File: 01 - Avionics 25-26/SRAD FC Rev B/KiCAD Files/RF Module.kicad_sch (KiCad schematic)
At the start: 0 parts

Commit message: Import CAD Files to make project symbol
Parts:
- added U2: SX1276IMLTRT, SX1276IMLTRT:QFN65P600X600X100-29N, symbol SX1276IMLTRT:SX1276IMLTRT
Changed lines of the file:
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@@
 	(generator_version "9.0")
 	(paper "A4")
+	(symbol
+		(lib_id "SX1276IMLTRT:SX1276IMLTRT")
+		(at 135.89 101.6 0)
+		(unit 1)
+		(exclude_from_sim no)
+		(in_bom yes)
+		(on_board yes)
+		(dnp no)
+		(fields_autoplaced yes)
+		(property "Reference" "U2"
+			(at 135.89 63.5 0)
+			(effects
+				(font
+					(size 1.27 1.27)
+				)
+			)
+		)
+		(property "Value" "SX1276IMLTRT"
+			(at 135.89 66.04 0)
+			(effects
+				(font
+					(size 1.27 1.27)
+				)
+			)
+		)
+		(property "Footprint" "SX1276IMLTRT:QFN65P600X600X100-29N"
+			(at 135.89 101.6 0)
+			(effects
+				(font
+					(size 1.27 1.27)
+				)
+				(justify bottom)
+				(hide yes)
+			)
+		)
+		(property "Datasheet" ""
+			(at 135.89 101.6 0)
+			(effects
+				(font
+					(size 1.27 1.27)
+				)
+				(hide yes)
+			)
+		)
+		(property "Description" ""
+			(at 135.89 101.6 0)
+			(effects
+				(font
+					(size 1.27 1.27)
+				)
+				(hide yes)
+			)
+		)
+		(property "PARTREV" "5"
+			(at 135.89 101.6 0)
+			(effects
+				(font
+					(size 1.27 1.27)
+				)
+				(justify bottom)
+				(hide yes)
+			)
+		)
+		(property "MANUFACTURER" "Semtech Corporation"
+			(at 135.89 101.6 0)
+			(effects
+				(font
+					(size 1.27 1.27)
+				)
+				(justify bottom)
+				(hide yes)
+			)
+		)
+		(property "STANDARD" "IPC-7351B"
+			(at 135.89 101.6 0)
+			(effects
+				(font
+					(size 1.27 1.27)
+				)
+				(justify bottom)
+				(hide yes)
+			)
+		)
+		(pin "29"
+		)
+		(pin "17"
+		)
+		(pin "18"
+		)
+		(pin "16"
+		)
+		(pin "1"
+		)
+		(pin "21"
+		)
+		(pin "7"
+		)
+		(pin "19"
+		)
+		(pin "27"
+		)
+		(pin "23"
+		)
+		(pin "26"
+		)
+		(pin "9"
+		)
+		(pin "6"
+		)
+		(pin "24"
+		)
+		(pin "12"
+		)
+		(pin "11"
+		)
+		(pin "10"
+		)
+		(pin "5"
+		)
+		(pin "3"
+		)
+		(pin "2"
+		)
+		(pin "15"
+		)
+		(pin "28"
+		)
+		(pin "14"
+		)
+		(pin "8"
+		)
+		(pin "20"
+		)
+		(pin "4"
+		)
+		(pin "25"
+		)
+		(pin "22"
+		)
+		(pin "13"
+		)
+		(instances
+			(project ""
+				(path "/1dd9e63a-24f2-43c6-ae21-66b89e6998f2/c560a1ce-e177-4cce-a057-3c7d08124339"
+					(reference "U2")
+					(unit 1)
+				)
+			)
+		)
+	)
 )

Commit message: Info to Storage and RF Module
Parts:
- RFModule: renamed from U2; Link (none) -> https://www.digikey.com/en/products/detail/semtech-corporat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
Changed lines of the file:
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@@
 		(dnp no)
 		(fields_autoplaced yes)
-		(property "Reference" "U2"
+		(property "Reference" "RFModule"
 			(at 135.89 63.5 0)
 			(effects
@@
 			)
 		)
-		(property "Datasheet" ""
+		(property "Datasheet" "https://semtech.my.salesforce.com/sfc/p/#E0000000JelG/a/2R0000001OKs/Bs97dmPXeatnbdoJNVMIDaKDlQz8q1N_gxDcgqi7g2o"
 			(at 135.89 101.6 0)
 			(effects
@@
 			)
 		)
-		(property "Description" ""
+		(property "Description" "SX1276/77/78/79 - 137 MHz to 1020 MHz Low Power Long Range Transceiver"
+			(at 135.89 101.6 0)
+			(effects
+				(font
+					(size 1.27 1.27)
+				)
+				(hide yes)
+			)
+		)
+		(property "Link" "https://www.digikey.com/en/products/detail/semtech-corporation/SX1276IMLTRT/4259565"
 			(at 135.89 101.6 0)
 			(effects
@@
 			(project ""
 				(path "/1dd9e63a-24f2-43c6-ae21-66b89e6998f2/c560a1ce-e177-4cce-a057-3c7d08124339"
-					(reference "U2")
+					(reference "RFModule")
 					(unit 1)
 				)

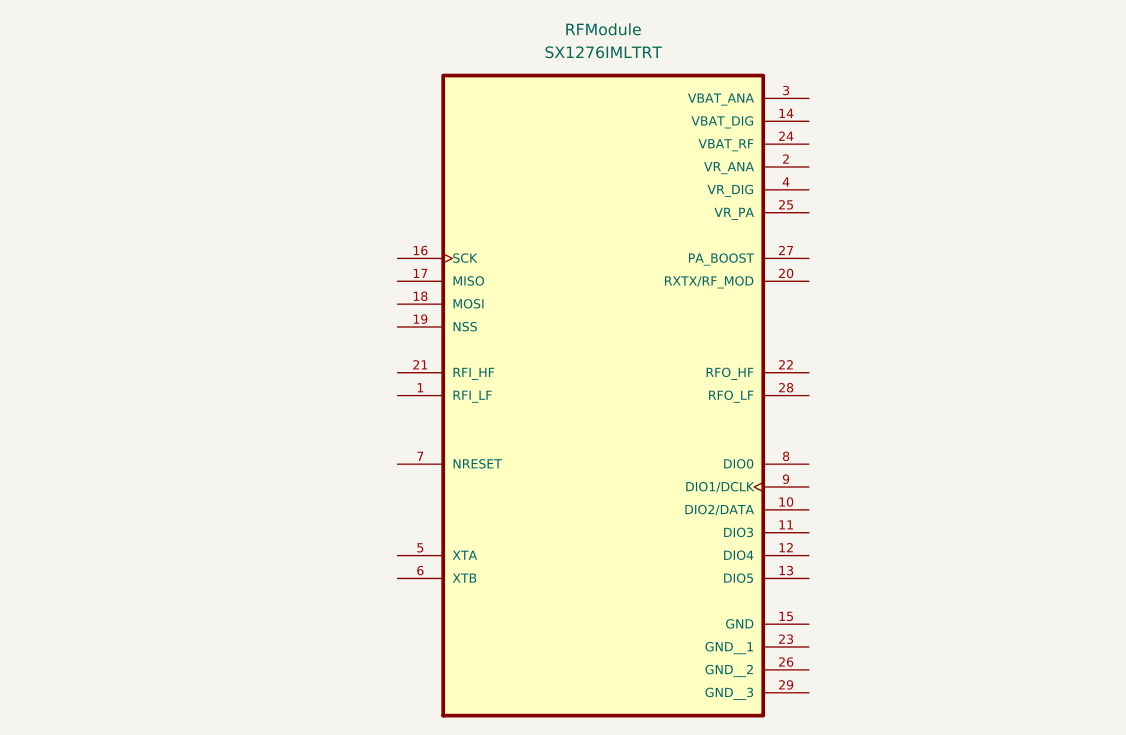
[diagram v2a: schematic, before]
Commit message: Added Storage and RF Module Circuits with Labels for Future Connects
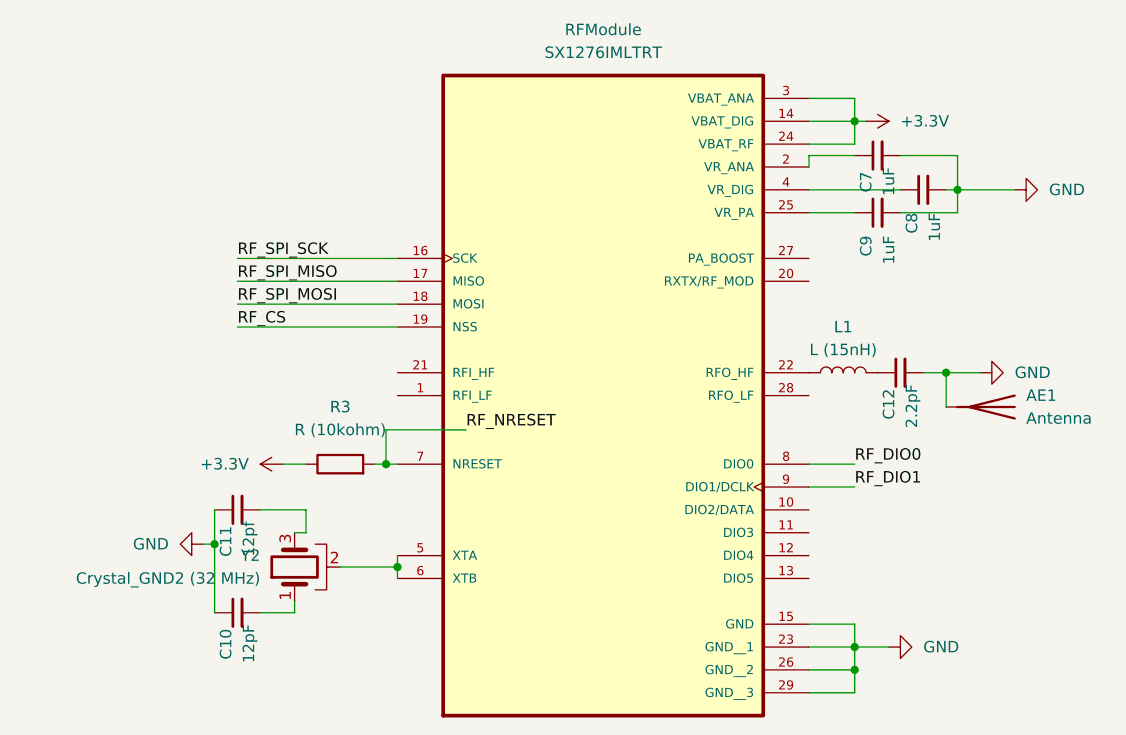
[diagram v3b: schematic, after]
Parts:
- added AE1: Antenna, symbol Device:Antenna
- added C10: 12pF, symbol Device:C_Small
- added C11: 12pf, symbol Device:C_Small
- added C12: 2.2pF, symbol Device:C_Small
- added C7, C8, C9: 1uF, symbol Device:C_Small
- added L1: L (15nH), symbol Device:L
- added R3: R (10kohm), symbol Device:R
- added Y2: Crystal_GND2 (32 MHz), symbol Device:Crystal_GND2
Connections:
- net +3.3V: now reaches RFModule.14 (VBAT_DIG)
- net +3.3V: now also RFModule.24 (VBAT_RF), RFModule.3 (VBAT_ANA), R3.1
- net GND: now reaches RFModule.15 (GND)
- net GND: now also RFModule.23 (GND__1), RFModule.26 (GND__2), RFModule.29 (GND__3), AE1.1 (A), C10.1, C11.1, C12.2, C7.2, C8.2, C9.2
- net RF_SPI_SCK: now reaches RFModule.16 (SCK)
- net RF_SPI_MISO: now reaches RFModule.17 (MISO)
- net RF_SPI_MOSI: now reaches RFModule.18 (MOSI)
- net RF_CS: now reaches RFModule.19 (NSS)
- net at RFModule.2 (VR_ANA): now also C7.1
- net at RFModule.22 (RFO_HF): now also L1.1
- net at RFModule.25 (VR_PA): now also C9.1
- net at RFModule.4 (VR_DIG): now also C8.1
- net at RFModule.5 (XTA): now also RFModule.6 (XTB), Y2.2
- net RF_NRESET: now reaches RFModule.7 (NRESET)
- net RF_NRESET: now also R3.2
- net RF_DIO0: now reaches RFModule.8 (DIO0)
- net RF_DIO1: now reaches RFModule.9 (DIO1/DCLK)
- new net: C11.2, Y2.3
- new net: C12.1, L1.2
- new net: C10.2, Y2.1

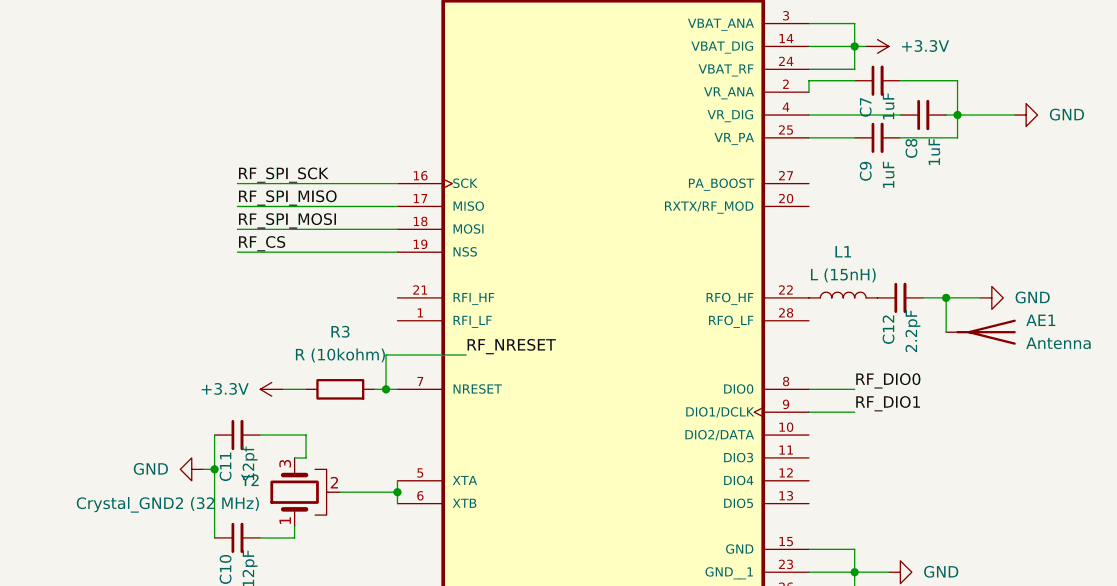
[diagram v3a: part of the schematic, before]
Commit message: Updated Sheet Pins
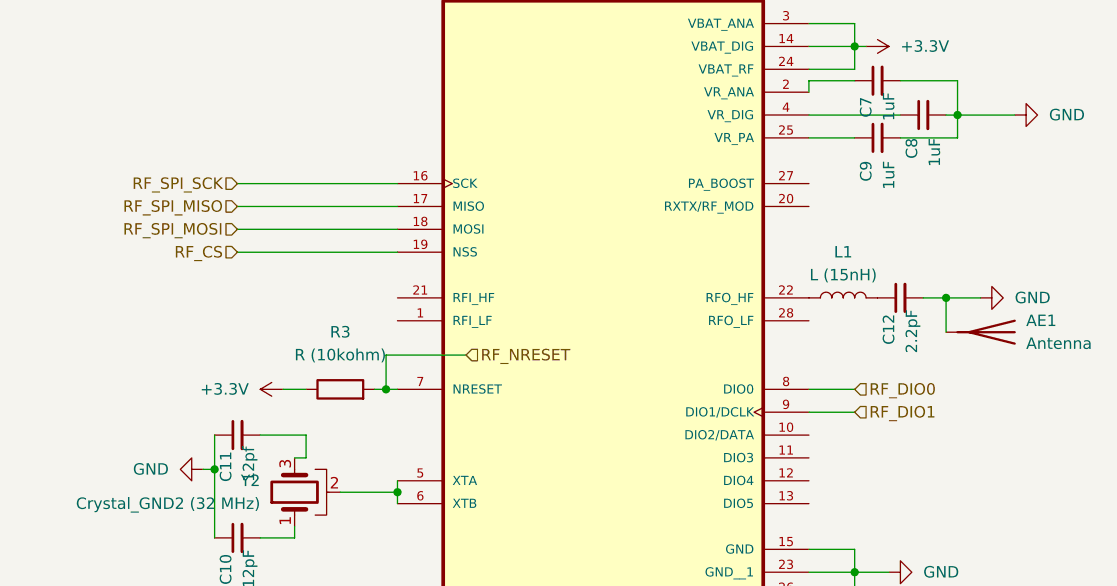
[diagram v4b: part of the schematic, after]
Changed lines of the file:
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@@
 		)
 	)
-	(label "RF_DIO0"
+	(hierarchical_label "RF_CS"
+		(shape input)
+		(at 95.25 96.52 180)
+		(effects
+			(font
+				(size 1.27 1.27)
+			)
+			(justify right)
+		)
+	)
+	(hierarchical_label "RF_DIO1"
+		(shape input)
+		(at 163.83 114.3 0)
+		(effects
+			(font
+				(size 1.27 1.27)
+			)
+			(justify left)
+		)
+	)
+	(hierarchical_label "RF_SPI_MOSI"
+		(shape input)
+		(at 95.25 93.98 180)
+		(effects
+			(font
+				(size 1.27 1.27)
+			)
+			(justify right)
+		)
+	)
+	(hierarchical_label "RF_DIO0"
+		(shape input)
 		(at 163.83 111.76 0)
 		(effects
@@
 				(size 1.27 1.27)
 			)
-			(justify left bottom)
+			(justify left)
 		)
 	)
-	(label "RF_CS"
-		(at 95.25 96.52 0)
+	(hierarchical_label "RF_SPI_SCK"
+		(shape input)
+		(at 95.25 88.9 180)
 		(effects
 			(font
 				(size 1.27 1.27)
 			)
-			(justify left bottom)
+			(justify right)
 		)
 	)
-	(label "RF_SPI_SCK"
-		(at 95.25 88.9 0)
+	(hierarchical_label "RF_SPI_MISO"
+		(shape input)
+		(at 95.25 91.44 180)
 		(effects
 			(font
 				(size 1.27 1.27)
 			)
-			(justify left bottom)
+			(justify right)
 		)
 	)
-	(label "RF_DIO1"
-		(at 163.83 114.3 0)
-		(effects
-			(font
-				(size 1.27 1.27)
-			)
-			(justify left bottom)
-		)
-	)
-	(label "RF_SPI_MISO"
-		(at 95.25 91.44 0)
-		(effects
-			(font
-				(size 1.27 1.27)
-			)
-			(justify left bottom)
-		)
-	)
-	(label "RF_NRESET"
+	(hierarchical_label "RF_NRESET"
+		(shape input)
 		(at 120.65 107.95 0)
 		(effects
@@
 				(size 1.27 1.27)
 			)
-			(justify left bottom)
+			(justify left)
 		)
 	)
-	(label "RF_SPI_MOSI"
-		(at 95.25 93.98 0)
-		(effects
-			(font
-				(size 1.27 1.27)
-			)
-			(justify left bottom)
-		)
-	)

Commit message: added power as hierarchical sheet pins
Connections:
- net +3.3V renamed RF_3.3V_POWER
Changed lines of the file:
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@@
+	)
+	(junction
+		(at 134.62 151.13)
+		(diameter 0)
+		(color 0 0 0 0)
 	)
 	(junction
@@
 	(wire
 		(pts
-			(xy 100.33 111.76) (xy 102.87 111.76)
-		)
-		(stroke
-			(width 0)
-			(type default)
-		)
-	)
-	(wire
-		(pts
 			(xy 111.76 107.95) (xy 111.76 111.76)
 		)
@@
 	(wire
 		(pts
+			(xy 199.39 151.13) (xy 134.62 151.13)
+		)
+		(stroke
+			(width 0)
+			(type default)
+		)
+	)
+	(wire
+		(pts
 			(xy 97.79 116.84) (xy 102.87 116.84)
 		)
@@
 	(wire
 		(pts
-			(xy 165.1 73.66) (xy 163.83 73.66)
+			(xy 163.83 73.66) (xy 199.39 73.66)
 		)
 		(stroke
@@
 	(wire
 		(pts
+			(xy 52.07 111.76) (xy 52.07 151.13)
+		)
+		(stroke
+			(width 0)
+			(type default)
+		)
+	)
+	(wire
+		(pts
 			(xy 91.44 120.65) (xy 92.71 120.65)
 		)
@@
 	(wire
 		(pts
+			(xy 199.39 73.66) (xy 199.39 151.13)
+		)
+		(stroke
+			(width 0)
+			(type default)
+		)
+	)
+	(wire
+		(pts
 			(xy 163.83 71.12) (xy 163.83 73.66)
 		)
@@
 	(wire
 		(pts
+			(xy 52.07 151.13) (xy 134.62 151.13)
+		)
+		(stroke
+			(width 0)
+			(type default)
+		)
+	)
+	(wire
+		(pts
+			(xy 52.07 111.76) (xy 102.87 111.76)
+		)
+		(stroke
+			(width 0)
+			(type default)
+		)
+	)
+	(wire
+		(pts
 			(xy 92.71 116.84) (xy 92.71 120.65)
 		)
@@
 		(pts
 			(xy 106.68 123.19) (xy 113.03 123.19)
+		)
+		(stroke
+			(width 0)
+			(type default)
+		)
+	)
+	(wire
+		(pts
+			(xy 134.62 151.13) (xy 134.62 161.29)
 		)
 		(stroke
@@
 		(shape input)
 		(at 95.25 96.52 180)
+		(effects
+			(font
+				(size 1.27 1.27)
+			)
+			(justify right)
+		)
+	)
+	(hierarchical_label "RF_3.3V_POWER"
+		(shape input)
+		(at 134.62 161.29 270)
 		(effects
 			(font
@@
 	)
 	(symbol
-		(lib_id "power:+3.3V")
-		(at 165.1 73.66 270)
-		(unit 1)
-		(exclude_from_sim no)
-		(in_bom yes)
-		(on_board yes)
-		(dnp no)
-		(fields_autoplaced yes)
-		(property "Reference" "#PWR013"
-			(at 161.29 73.66 0)
-			(effects
-				(font
-					(size 1.27 1.27)
-				)
-				(hide yes)
-			)
-		)
-		(property "Value" "+3.3V"
-			(at 168.91 73.6599 90)
-			(effects
-				(font
-					(size 1.27 1.27)
-				)
-				(justify left)
-			)
-		)
-		(property "Footprint" ""
-			(at 165.1 73.66 0)
-			(effects
-				(font
-					(size 1.27 1.27)
-				)
-				(hide yes)
-			)
-		)
-		(property "Datasheet" ""
-			(at 165.1 73.66 0)
-			(effects
-				(font
-					(size 1.27 1.27)
-				)
-				(hide yes)
-			)
-		)
-		(property "Description" "Power symbol creates a global label with name \"+3.3V\""
-			(at 165.1 73.66 0)
-			(effects
-				(font
-					(size 1.27 1.27)
-				)
-				(hide yes)
-			)
-		)
-		(pin "1"
-		)
-		(instances
-			(project ""
-				(path "/1dd9e63a-24f2-43c6-ae21-66b89e6998f2/c560a1ce-e177-4cce-a057-3c7d08124339"
-					(reference "#PWR013")
-					(unit 1)
-				)
-			)
-		)
-	)
-	(symbol
 		(lib_id "Device:Crystal_GND2")
 		(at 101.6 123.19 90)
@@
 					(unit 1)
 				)
-			)
-		)
-	)
-	(symbol
-		(lib_id "power:+3.3V")
-		(at 100.33 111.76 90)
-		(unit 1)
-		(exclude_from_sim no)
-		(in_bom yes)
-		(on_board yes)
-		(dnp no)
-		(fields_autoplaced yes)
-		(property "Reference" "#PWR017"
-			(at 104.14 111.76 0)
-			(effects
-				(font
-					(size 1.27 1.27)
-				)
-				(hide yes)
-			)
-		)
-		(property "Value" "+3.3V"
-			(at 96.52 111.7599 90)
-			(effects
-				(font
-					(size 1.27 1.27)
-				)
-				(justify left)
-			)
-		)
-		(property "Footprint" ""
-			(at 100.33 111.76 0)
-			(effects
-				(font
-					(size 1.27 1.27)
-				)
-				(hide yes)
-			)
-		)
-		(property "Datasheet" ""
-			(at 100.33 111.76 0)
-			(effects
-				(font
-					(size 1.27 1.27)
-				)
-				(hide yes)
-			)
-		)
-		(property "Description" "Power symbol creates a global label with name \"+3.3V\""
-			(at 100.33 111.76 0)
-			(effects
-				(font
-					(size 1.27 1.27)
-				)
-				(hide yes)
-			)
-		)
-		(pin "1"
-		)
-		(instances
-			(project "SRAD FC Rev B"
-				(path "/1dd9e63a-24f2-43c6-ae21-66b89e6998f2/c560a1ce-e177-4cce-a057-3c7d08124339"
-					(reference "#PWR017")
-					(unit 1)
-				)

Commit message: general fixes for sheet sheet, ERC error fixes
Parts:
- renumbered R3 to R103
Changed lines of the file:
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@@
 		(dnp no)
 		(fields_autoplaced yes)
-		(property "Reference" "R3"
+		(property "Reference" "R103"
 			(at 106.68 105.41 90)
 			(effects
@@
 			(project ""
 				(path "/1dd9e63a-24f2-43c6-ae21-66b89e6998f2/c560a1ce-e177-4cce-a057-3c7d08124339"
-					(reference "R3")
+					(reference "R103")
 					(unit 1)
 				)

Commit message: set up power conversion, wired power to mcu
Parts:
- removed RFModule: SX1276IMLTRT, SX1276IMLTRT:QFN65P600X600X100-29N, symbol SX1276IMLTRT:SX1276IMLTRT
- added U7: SX1276IMLTRT, SX1276IMLTRT:QFN65P600X600X100-29N, symbol SX1276IMLTRT:SX1276IMLTRT
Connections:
- net GND: now also U7.15 (GND), U7.23 (GND__1), U7.26 (GND__2), U7.29 (GND__3)
- net RF_3.3V_POWER: now also U7.14 (VBAT_DIG), U7.24 (VBAT_RF), U7.3 (VBAT_ANA)
- net RF_CS: now also U7.19 (NSS)
- net RF_DIO0: now also U7.8 (DIO0)
- net RF_DIO1: now also U7.9 (DIO1/DCLK)
- net RF_NRESET: now also U7.7 (NRESET)
- net RF_SPI_MISO: now also U7.17 (MISO)
- net RF_SPI_MOSI: now also U7.18 (MOSI)
- net RF_SPI_SCK: now also U7.16 (SCK)
- net at L1.1: now also U7.22 (RFO_HF)
- net at C7.1: now also U7.2 (VR_ANA)
- net at Y2.2: now also U7.5 (XTA), U7.6 (XTB)
- net at C9.1: now also U7.25 (VR_PA)
- net at C8.1: now also U7.4 (VR_DIG)
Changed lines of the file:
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@@
+	)
+	(symbol
+		(lib_id "SX1276IMLTRT:SX1276IMLTRT")
+		(at 135.89 101.6 0)
+		(unit 1)
+		(exclude_from_sim no)
+		(in_bom yes)
+		(on_board yes)
+		(dnp no)
+		(fields_autoplaced yes)
+		(property "Reference" "U7"
+			(at 135.89 63.5 0)
+			(effects
+				(font
+					(size 1.27 1.27)
+				)
+			)
+		)
+		(property "Value" "SX1276IMLTRT"
+			(at 135.89 66.04 0)
+			(effects
+				(font
+					(size 1.27 1.27)
+				)
+			)
+		)
+		(property "Footprint" "SX1276IMLTRT:QFN65P600X600X100-29N"
+			(at 135.89 101.6 0)
+			(effects
+				(font
+					(size 1.27 1.27)
+				)
+				(justify bottom)
+				(hide yes)
+			)
+		)
+		(property "Datasheet" ""
+			(at 135.89 101.6 0)
+			(effects
+				(font
+					(size 1.27 1.27)
+				)
+				(hide yes)
+			)
+		)
+		(property "Description" ""
+			(at 135.89 101.6 0)
+			(effects
+				(font
+					(size 1.27 1.27)
+				)
+				(hide yes)
+			)
+		)
+		(property "PARTREV" "5"
+			(at 135.89 101.6 0)
+			(effects
+				(font
+					(size 1.27 1.27)
+				)
+				(justify bottom)
+				(hide yes)
+			)
+		)
+		(property "MANUFACTURER" "Semtech Corporation"
+			(at 135.89 101.6 0)
+			(effects
+				(font
+					(size 1.27 1.27)
+				)
+				(justify bottom)
+				(hide yes)
+			)
+		)
+		(property "STANDARD" "IPC-7351B"
+			(at 135.89 101.6 0)
+			(effects
+				(font
+					(size 1.27 1.27)
+				)
+				(justify bottom)
+				(hide yes)
+			)
+		)
+		(pin "19"
+		)
+		(pin "5"
+		)
+		(pin "17"
+		)
+		(pin "12"
+		)
+		(pin "18"
+		)
+		(pin "11"
+		)
+		(pin "13"
+		)
+		(pin "29"
+		)
+		(pin "1"
+		)
+		(pin "8"
+		)
+		(pin "9"
+		)
+		(pin "7"
+		)
+		(pin "20"
+		)
+		(pin "24"
+		)
+		(pin "16"
+		)
+		(pin "4"
+		)
+		(pin "25"
+		)
+		(pin "2"
+		)
+		(pin "27"
+		)
+		(pin "22"
+		)
+		(pin "21"
+		)
+		(pin "14"
+		)
+		(pin "28"
+		)
+		(pin "10"
+		)
+		(pin "6"
+		)
+		(pin "3"
+		)
+		(pin "23"
+		)
+		(pin "26"
+		)
+		(pin "15"
+		)
+		(instances
+			(project ""
+				(path "/1dd9e63a-24f2-43c6-ae21-66b89e6998f2/c560a1ce-e177-4cce-a057-3c7d08124339"
+					(reference "U7")
+					(unit 1)
+				)
+			)
+		)
 	)
 	(symbol
@@
 					(unit 1)
 				)
-			)
-		)
-	)
-	(symbol
-		(lib_id "SX1276IMLTRT:SX1276IMLTRT")
-		(at 135.89 101.6 0)
-		(unit 1)
-		(exclude_from_sim no)
-		(in_bom yes)
-		(on_board yes)
-		(dnp no)
-		(fields_autoplaced yes)
-		(property "Reference" "RFModule"
-			(at 135.89 63.5 0)
-			(effects
-				(font
-					(size 1.27 1.27)
-				)
-			)
-		)
-		(property "Value" "SX1276IMLTRT"
-			(at 135.89 66.04 0)
-			(effects
-				(font
-					(size 1.27 1.27)
-				)
-			)
-		)
-		(property "Footprint" "SX1276IMLTRT:QFN65P600X600X100-29N"
-			(at 135.89 101.6 0)
-			(effects
-				(font
-					(size 1.27 1.27)
-				)
-				(justify bottom)
-				(hide yes)
-			)
-		)
-		(property "Datasheet" "https://semtech.my.salesforce.com/sfc/p/#E0000000JelG/a/2R0000001OKs/Bs97dmPXeatnbdoJNVMIDaKDlQz8q1N_gxDcgqi7g2o"
-			(at 135.89 101.6 0)
-			(effects
-				(font
-					(size 1.27 1.27)
-				)
-				(hide yes)
-			)
-		)
-		(property "Description" "SX1276/77/78/79 - 137 MHz to 1020 MHz Low Power Long Range Transceiver"
-			(at 135.89 101.6 0)
-			(effects
-				(font
-					(size 1.27 1.27)
-				)
-				(hide yes)
-			)
-		)
-		(property "Link" "https://www.digikey.com/en/products/detail/semtech-corporation/SX1276IMLTRT/4259565"
-			(at 135.89 101.6 0)
-			(effects
-				(font
-					(size 1.27 1.27)
-				)
-				(hide yes)
-			)
-		)
-		(property "PARTREV" "5"
-			(at 135.89 101.6 0)
-			(effects
-				(font
-					(size 1.27 1.27)
-				)
-				(justify bottom)
-				(hide yes)
-			)
-		)
-		(property "MANUFACTURER" "Semtech Corporation"
-			(at 135.89 101.6 0)
-			(effects
-				(font
-					(size 1.27 1.27)
-				)
-				(justify bottom)
-				(hide yes)
-			)
-		)
-		(property "STANDARD" "IPC-7351B"
-			(at 135.89 101.6 0)
-			(effects
-				(font
-					(size 1.27 1.27)
-				)
-				(justify bottom)
-				(hide yes)
-			)
-		)
-		(pin "29"
-		)
-		(pin "17"
-		)
-		(pin "18"
-		)
-		(pin "16"
-		)
-		(pin "1"
-		)
-		(pin "21"
-		)
-		(pin "7"
-		)
-		(pin "19"
-		)
-		(pin "27"
-		)
-		(pin "23"
-		)
-		(pin "26"
-		)
-		(pin "9"
-		)
-		(pin "6"
-		)
-		(pin "24"
-		)
-		(pin "12"
-		)
-		(pin "11"
-		)
-		(pin "10"
-		)
-		(pin "5"
-		)
-		(pin "3"
-		)
-		(pin "2"
-		)
-		(pin "15"
-		)
-		(pin "28"
-		)
-		(pin "14"
-		)
-		(pin "8"
-		)
-		(pin "20"
-		)
-		(pin "4"
-		)
-		(pin "25"
-		)
-		(pin "22"
-		)
-		(pin "13"
-		)
-		(instances
-			(project ""
-				(path "/1dd9e63a-24f2-43c6-ae21-66b89e6998f2/c560a1ce-e177-4cce-a057-3c7d08124339"
-					(reference "RFModule")
-					(unit 1)
-				)
